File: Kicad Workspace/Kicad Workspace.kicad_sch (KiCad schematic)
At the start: 0 parts

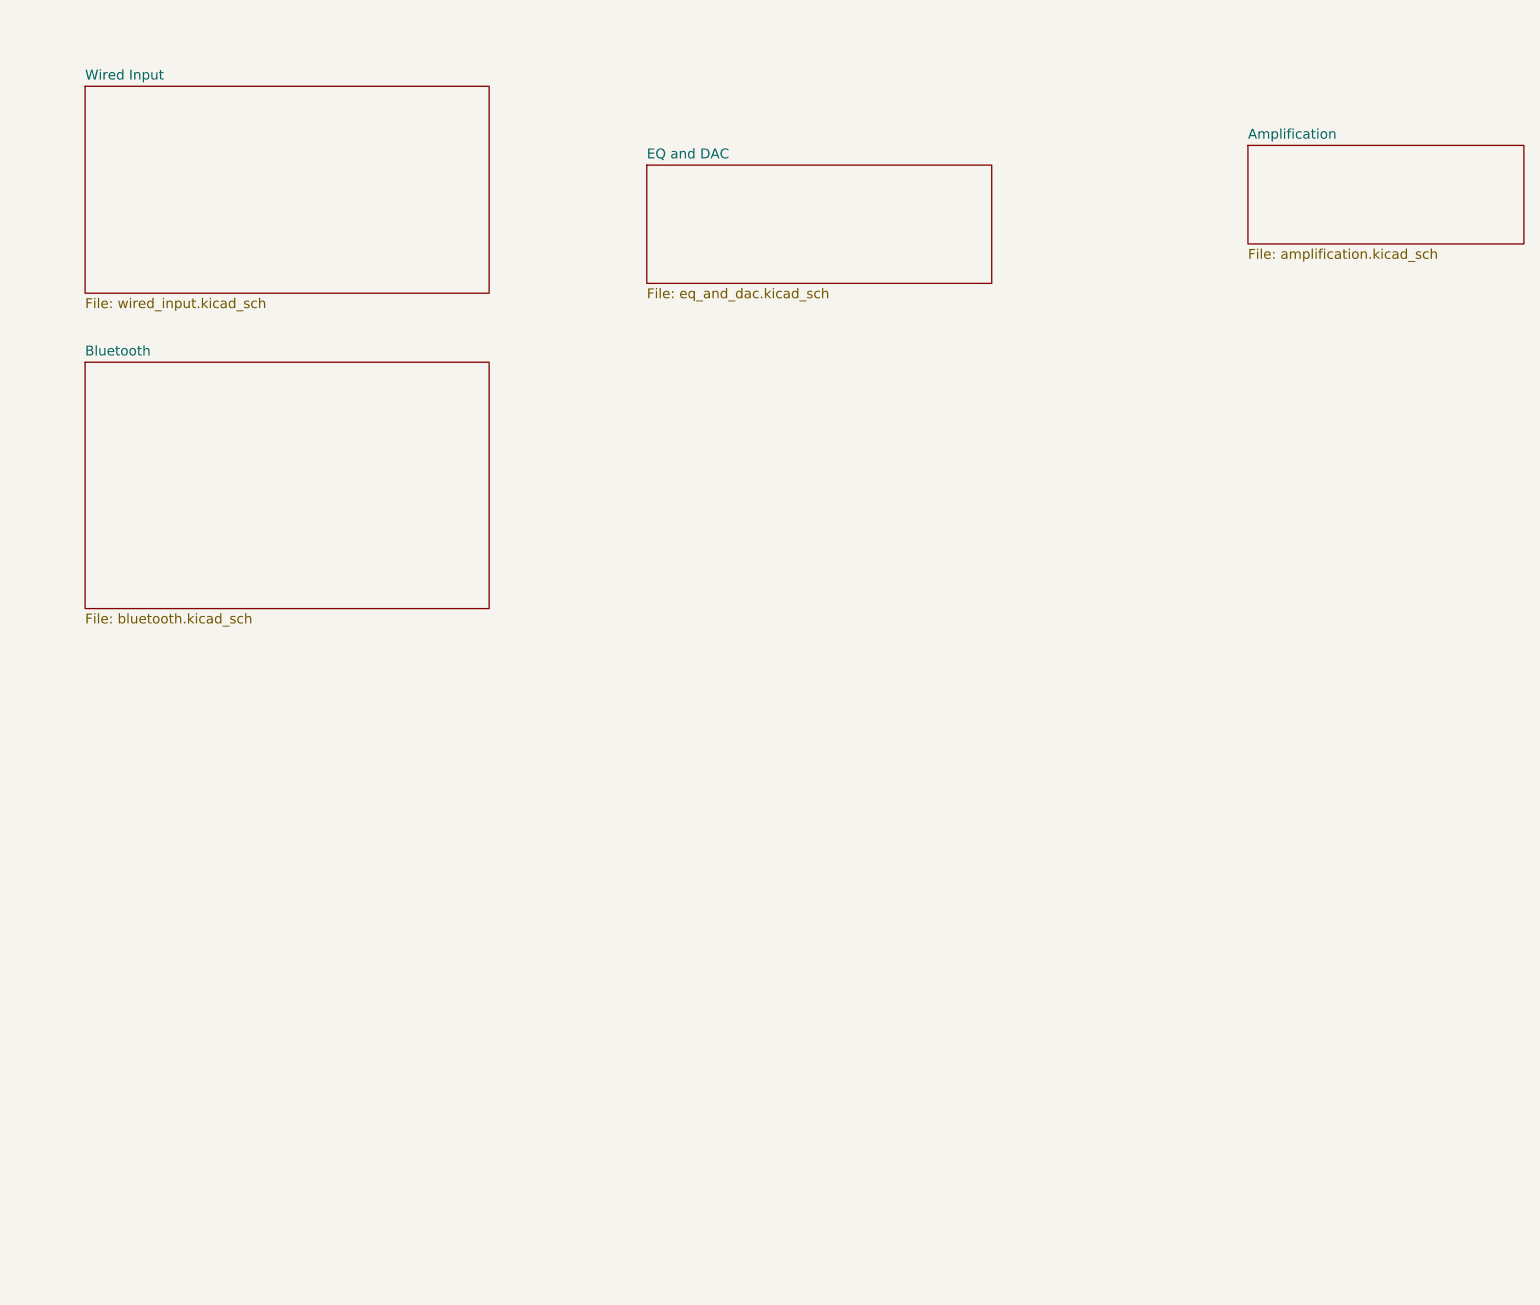
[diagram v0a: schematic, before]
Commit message: Wire input (ADC) schematics done
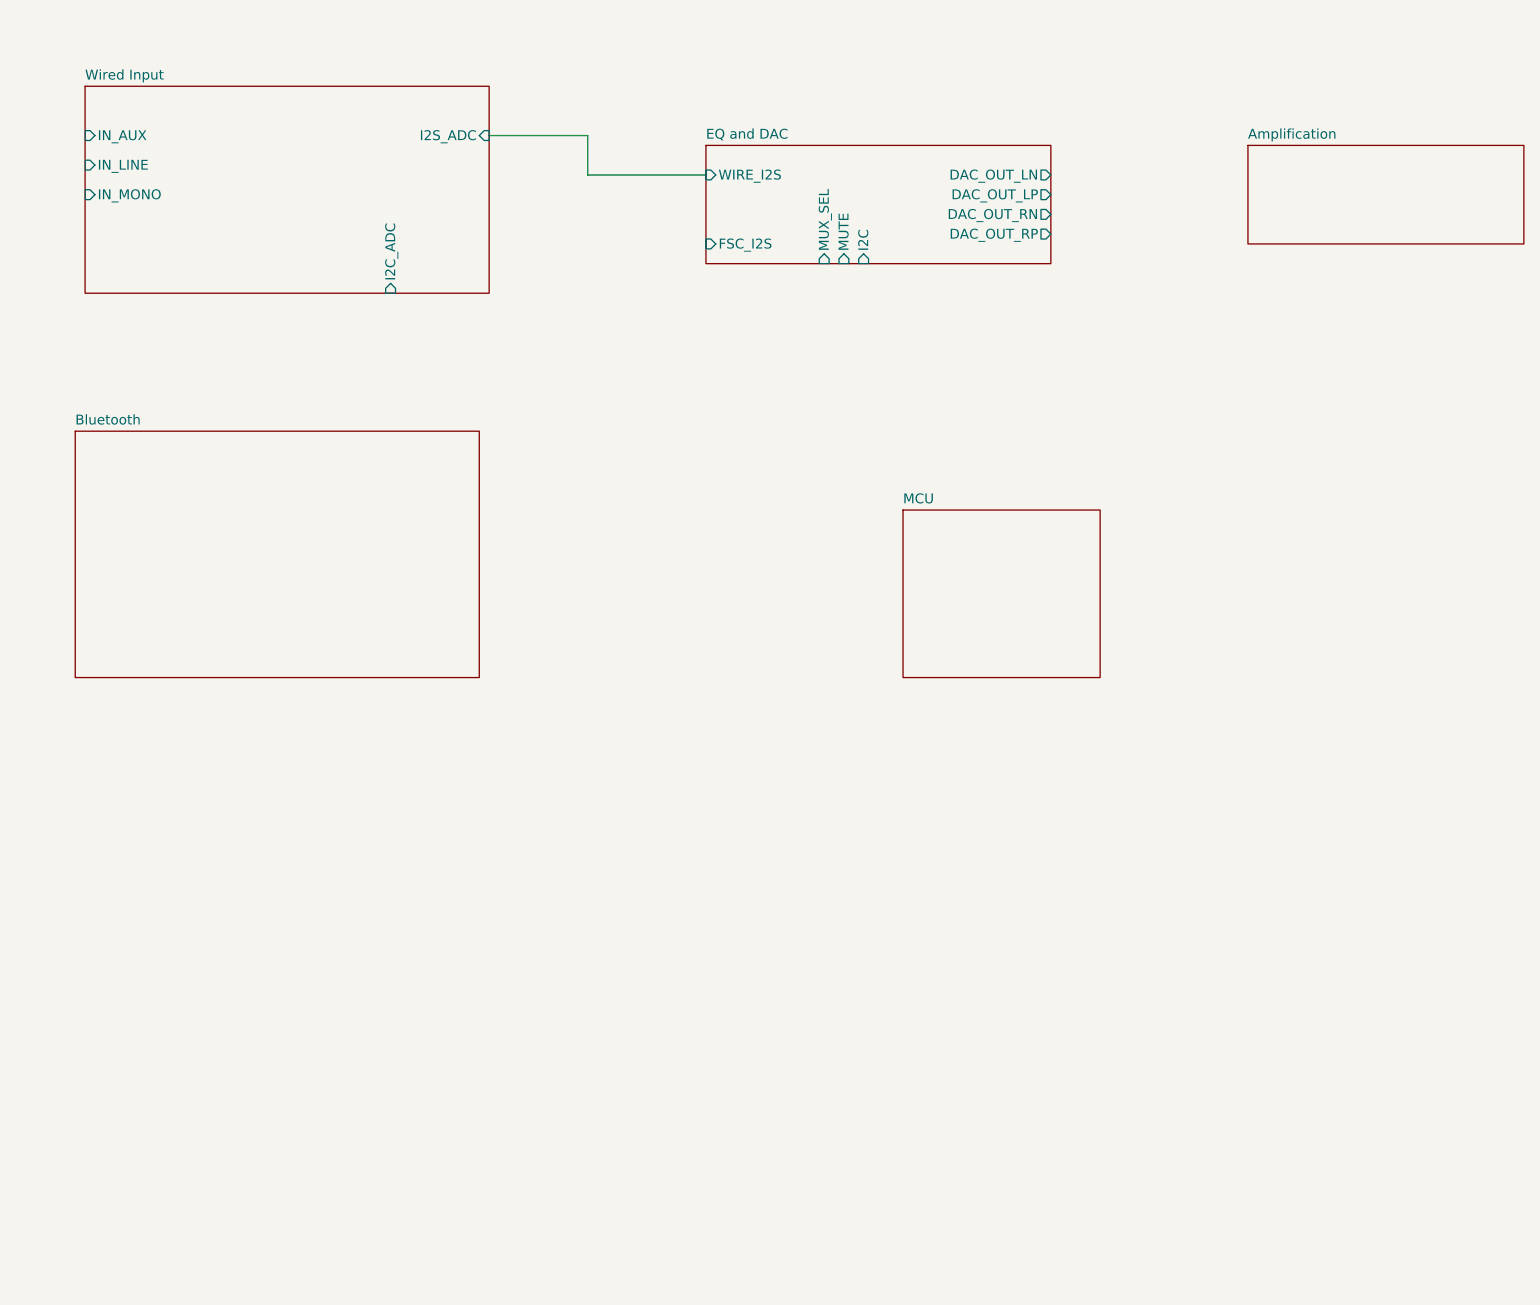
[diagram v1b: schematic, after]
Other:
- added sheet MCU (mcu.kicad_sch)
- sheet EQ and DAC ports: added DAC_OUT_LN, DAC_OUT_LP, DAC_OUT_RN, DAC_OUT_RP, FSC_I2S, I2C, MUTE, MUX_SEL, WIRE_I2S; removed none
- sheet Wired Input ports: added I2C_ADC, I2S_ADC, IN_AUX, IN_LINE, IN_MONO; removed none
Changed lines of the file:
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@@
 	(generator_version "10.0")
 	(paper "A4")
+	(wire
+		(pts
+			(xy 80.01 31.75) (xy 92.71 31.75)
+		)
+		(stroke
+			(width 0)
+			(type default)
+		)
+	)
+	(wire
+		(pts
+			(xy 92.71 36.83) (xy 107.95 36.83)
+		)
+		(stroke
+			(width 0)
+			(type default)
+		)
+	)
+	(wire
+		(pts
+			(xy 92.71 31.75) (xy 92.71 36.83)
+		)
+		(stroke
+			(width 0)
+			(type default)
+		)
+	)
 	(sheet
 		(at 27.94 25.4)
@@
 		(property "Sheetfile" "wired_input.kicad_sch"
 			(at 27.94 52.6546 0)
+			(hide yes)
 			(show_name no)
 			(do_not_autoplace no)
@@
 				)
 				(justify left top)
+			)
+		)
+		(pin "I2C_ADC" input
+			(at 67.31 52.07 270)
+			(effects
+				(font
+					(size 1.27 1.27)
+				)
+				(justify left)
+			)
+		)
+		(pin "I2S_ADC" input
+			(at 80.01 31.75 0)
+			(effects
+				(font
+					(size 1.27 1.27)
+				)
+				(justify right)
+			)
+		)
+		(pin "IN_AUX" input
+			(at 27.94 31.75 180)
+			(effects
+				(font
+					(size 1.27 1.27)
+				)
+				(justify left)
+			)
+		)
+		(pin "IN_LINE" input
+			(at 27.94 35.56 180)
+			(effects
+				(font
+					(size 1.27 1.27)
+				)
+				(justify left)
+			)
+		)
+		(pin "IN_MONO" input
+			(at 27.94 39.37 180)
+			(effects
+				(font
+					(size 1.27 1.27)
+				)
+				(justify left)
 			)
 		)
@@
 	)
 	(sheet
-		(at 100.33 35.56)
+		(at 107.95 33.02)
 		(size 44.45 15.24)
 		(exclude_from_sim no)
@@
 		)
 		(property "Sheetname" "EQ and DAC"
-			(at 100.33 34.8484 0)
+			(at 107.95 32.3084 0)
 			(show_name no)
 			(do_not_autoplace no)
@@
 		)
 		(property "Sheetfile" "eq_and_dac.kicad_sch"
-			(at 100.33 51.3846 0)
+			(at 107.95 48.8446 0)
+			(hide yes)
 			(show_name no)
 			(do_not_autoplace no)
@@
 				)
 				(justify left top)
+			)
+		)
+		(pin "DAC_OUT_LN" output
+			(at 152.4 36.83 0)
+			(effects
+				(font
+					(size 1.27 1.27)
+				)
+				(justify right)
+			)
+		)
+		(pin "DAC_OUT_LP" output
+			(at 152.4 39.37 0)
+			(effects
+				(font
+					(size 1.27 1.27)
+				)
+				(justify right)
+			)
+		)
+		(pin "DAC_OUT_RN" output
+			(at 152.4 41.91 0)
+			(effects
+				(font
+					(size 1.27 1.27)
+				)
+				(justify right)
+			)
+		)
+		(pin "DAC_OUT_RP" output
+			(at 152.4 44.45 0)
+			(effects
+				(font
+					(size 1.27 1.27)
+				)
+				(justify right)
+			)
+		)
+		(pin "FSC_I2S" input
+			(at 107.95 45.72 180)
+			(effects
+				(font
+					(size 1.27 1.27)
+				)
+				(justify left)
+			)
+		)
+		(pin "I2C" input
+			(at 128.27 48.26 270)
+			(effects
+				(font
+					(size 1.27 1.27)
+				)
+				(justify left)
+			)
+		)
+		(pin "MUTE" input
+			(at 125.73 48.26 270)
+			(effects
+				(font
+					(size 1.27 1.27)
+				)
+				(justify left)
+			)
+		)
+		(pin "MUX_SEL" input
+			(at 123.19 48.26 270)
+			(effects
+				(font
+					(size 1.27 1.27)
+				)
+				(justify left)
+			)
+		)
+		(pin "WIRE_I2S" input
+			(at 107.95 36.83 180)
+			(effects
+				(font
+					(size 1.27 1.27)
+				)
+				(justify left)
 			)
 		)
@@
 	)
 	(sheet
-		(at 27.94 60.96)
+		(at 133.35 80.01)
+		(size 25.4 21.59)
+		(exclude_from_sim no)
+		(in_bom yes)
+		(on_board yes)
+		(dnp no)
+		(fields_autoplaced yes)
+		(stroke
+			(width 0.1524)
+			(type solid)
+		)
+		(fill
+			(color 0 0 0 0)
+		)
+		(property "Sheetname" "MCU"
+			(at 133.35 79.2984 0)
+			(show_name no)
+			(do_not_autoplace no)
+			(effects
+				(font
+					(size 1.27 1.27)
+				)
+				(justify left bottom)
+			)
+		)
+		(property "Sheetfile" "mcu.kicad_sch"
+			(at 133.35 102.1846 0)
+			(hide yes)
+			(show_name no)
+			(do_not_autoplace no)
+			(effects
+				(font
+					(size 1.27 1.27)
+				)
+				(justify left top)
+			)
+		)
+		(instances
+			(project "Kicad Workspace"
+				(path "/7c7afbb1-f4ab-42aa-9bad-41afd809eff4"
+					(page "6")
+				)
+			)
+		)
+	)
+	(sheet
+		(at 26.67 69.85)
 		(size 52.07 31.75)
 		(exclude_from_sim no)
@@
 		)
 		(property "Sheetname" "Bluetooth"
-			(at 27.94 60.2484 0)
+			(at 26.67 69.1384 0)
 			(show_name no)
 			(do_not_autoplace no)
@@
 		)
 		(property "Sheetfile" "bluetooth.kicad_sch"
-			(at 27.94 93.2946 0)
+			(at 26.67 102.1846 0)
+			(hide yes)
 			(show_name no)
 			(do_not_autoplace no)
@@
 		(property "Sheetfile" "amplification.kicad_sch"
 			(at 177.8 46.3046 0)
-			(show_name no)
-			(do_not_autoplace no)
+			(hide yes)
+			(show_name no)
+			(do_not_autoplace no)

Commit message: pro and sch update
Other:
- sheet Bluetooth ports: added BT_I2S, BT_RESET, BT_UART; removed none
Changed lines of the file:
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@@
+	(wire
+		(pts
+			(xy 92.71 45.72) (xy 107.95 45.72)
+		)
+		(stroke
+			(width 0)
+			(type default)
+		)
+	)
 	(wire
 		(pts
 			(xy 92.71 31.75) (xy 92.71 36.83)
+		)
+		(stroke
+			(width 0)
+			(type default)
+		)
+	)
+	(wire
+		(pts
+			(xy 78.74 73.66) (xy 92.71 73.66)
+		)
+		(stroke
+			(width 0)
+			(type default)
+		)
+	)
+	(wire
+		(pts
+			(xy 92.71 73.66) (xy 92.71 45.72)
 		)
 		(stroke
@@
 			)
 		)
+		(pin "BT_I2S" output
+			(at 78.74 73.66 0)
+			(effects
+				(font
+					(size 1.27 1.27)
+				)
+				(justify right)
+			)
+		)
+		(pin "BT_RESET" input
+			(at 78.74 99.06 0)
+			(effects
+				(font
+					(size 1.27 1.27)
+				)
+				(justify right)
+			)
+		)
+		(pin "BT_UART" input
+			(at 78.74 96.52 0)
+			(effects
+				(font
+					(size 1.27 1.27)
+				)
+				(justify right)
+			)
+		)
 		(instances
 			(project "Kicad Workspace"
@@
 	)
 	(sheet
-		(at 177.8 33.02)
+		(at 173.99 36.83)
 		(size 35.56 12.7)
 		(exclude_from_sim no)
@@
 		)
 		(property "Sheetname" "Amplification"
-			(at 177.8 32.3084 0)
+			(at 173.99 36.1184 0)
 			(show_name no)
 			(do_not_autoplace no)
@@
 		)
 		(property "Sheetfile" "amplification.kicad_sch"
-			(at 177.8 46.3046 0)
+			(at 173.99 50.1146 0)
 			(hide yes)
 			(show_name no)

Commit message: project update
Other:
- sheet Amplification ports: added CLIP, FAULT, RESET; removed none
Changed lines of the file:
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@@
+			)
+		)
+		(pin "CLIP" output
+			(at 186.69 49.53 270)
+			(effects
+				(font
+					(size 1.27 1.27)
+				)
+				(justify left)
+			)
+		)
+		(pin "FAULT" output
+			(at 189.23 49.53 270)
+			(effects
+				(font
+					(size 1.27 1.27)
+				)
+				(justify left)
+			)
+		)
+		(pin "RESET" input
+			(at 191.77 49.53 270)
+			(effects
+				(font
+					(size 1.27 1.27)
+				)
+				(justify left)
 			)
 		)

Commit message: feat: project global
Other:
- sheet Amplification ports: added IN_L+, IN_L-, IN_R+, IN_R-, L+, L-, R+, R-; removed none
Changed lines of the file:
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@@
 	)
 	(sheet
-		(at 173.99 36.83)
-		(size 35.56 12.7)
+		(at 170.18 27.94)
+		(size 27.94 20.32)
 		(exclude_from_sim no)
 		(in_bom yes)
@@
 		)
 		(property "Sheetname" "Amplification"
-			(at 173.99 36.1184 0)
+			(at 170.18 27.2284 0)
 			(show_name no)
 			(do_not_autoplace no)
@@
 		)
 		(property "Sheetfile" "amplification.kicad_sch"
-			(at 173.99 50.1146 0)
+			(at 170.18 48.8446 0)
 			(hide yes)
 			(show_name no)
@@
 		)
 		(pin "CLIP" output
-			(at 186.69 49.53 270)
+			(at 182.88 48.26 270)
 			(effects
 				(font
@@
 		)
 		(pin "FAULT" output
-			(at 189.23 49.53 270)
+			(at 185.42 48.26 270)
 			(effects
 				(font
@@
 		)
 		(pin "RESET" input
-			(at 191.77 49.53 270)
+			(at 187.96 48.26 270)
 			(effects
 				(font
+					(size 1.27 1.27)
+				)
+				(justify left)
+			)
+		)
+		(pin "IN_L-" input
+			(at 170.18 33.02 180)
+			(effects
+				(font
+					(size 1.27 1.27)
+				)
+				(justify left)
+			)
+		)
+		(pin "IN_R+" input
+			(at 170.18 38.1 180)
+			(effects
+				(font
+					(size 1.27 1.27)
+				)
+				(justify left)
+			)
+		)
+		(pin "IN_R-" input
+			(at 170.18 40.64 180)
+			(effects
+				(font
+					(size 1.27 1.27)
+				)
+				(justify left)
+			)
+		)
+		(pin "L+" output
+			(at 198.12 30.48 0)
+			(effects
+				(font
+					(size 1.27 1.27)
+				)
+				(justify right)
+			)
+		)
+		(pin "L-" output
+			(at 198.12 33.02 0)
+			(effects
+				(font
+					(size 1.27 1.27)
+				)
+				(justify right)
+			)
+		)
+		(pin "R+" output
+			(at 198.12 38.1 0)
+			(effects
+				(font
+					(size 1.27 1.27)
+				)
+				(justify right)
+			)
+		)
+		(pin "R-" output
+			(at 198.12 40.64 0)
+			(effects
+				(font
+					(size 1.27 1.27)
+				)
+				(justify right)
+			)
+		)
+		(pin "IN_L+" input
+			(at 170.18 30.48 180)
+			(effects
+				(font

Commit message: project update
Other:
- added sheet Alimentation (alimentation.kicad_sch)
- sheet EQ and DAC ports: added L+, L-, R+, R-; removed DAC_OUT_LN, DAC_OUT_LP, DAC_OUT_RN, DAC_OUT_RP
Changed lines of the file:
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@@
+	(wire
+		(pts
+			(xy 152.4 35.56) (xy 170.18 35.56)
+		)
+		(stroke
+			(width 0)
+			(type default)
+		)
+	)
 	(wire
 		(pts
@@
 	(wire
 		(pts
+			(xy 152.4 43.18) (xy 170.18 43.18)
+		)
+		(stroke
+			(width 0)
+			(type default)
+		)
+	)
+	(wire
+		(pts
+			(xy 152.4 38.1) (xy 170.18 38.1)
+		)
+		(stroke
+			(width 0)
+			(type default)
+		)
+	)
+	(wire
+		(pts
 			(xy 92.71 31.75) (xy 92.71 36.83)
 		)
@@
 		(pts
 			(xy 78.74 73.66) (xy 92.71 73.66)
+		)
+		(stroke
+			(width 0)
+			(type default)
+		)
+	)
+	(wire
+		(pts
+			(xy 152.4 45.72) (xy 170.18 45.72)
 		)
 		(stroke
@@
 			)
 		)
-		(pin "DAC_OUT_LN" output
-			(at 152.4 36.83 0)
-			(effects
-				(font
-					(size 1.27 1.27)
-				)
-				(justify right)
-			)
-		)
-		(pin "DAC_OUT_LP" output
-			(at 152.4 39.37 0)
-			(effects
-				(font
-					(size 1.27 1.27)
-				)
-				(justify right)
-			)
-		)
-		(pin "DAC_OUT_RN" output
-			(at 152.4 41.91 0)
-			(effects
-				(font
-					(size 1.27 1.27)
-				)
-				(justify right)
-			)
-		)
-		(pin "DAC_OUT_RP" output
-			(at 152.4 44.45 0)
-			(effects
-				(font
-					(size 1.27 1.27)
-				)
-				(justify right)
-			)
-		)
 		(pin "FSC_I2S" input
 			(at 107.95 45.72 180)
@@
 				)
 				(justify left)
+			)
+		)
+		(pin "L+" output
+			(at 152.4 35.56 0)
+			(effects
+				(font
+					(size 1.27 1.27)
+				)
+				(justify right)
+			)
+		)
+		(pin "L-" output
+			(at 152.4 38.1 0)
+			(effects
+				(font
+					(size 1.27 1.27)
+				)
+				(justify right)
+			)
+		)
+		(pin "R+" output
+			(at 152.4 43.18 0)
+			(effects
+				(font
+					(size 1.27 1.27)
+				)
+				(justify right)
+			)
+		)
+		(pin "R-" output
+			(at 152.4 45.72 0)
+			(effects
+				(font
+					(size 1.27 1.27)
+				)
+				(justify right)
 			)
 		)
@@
 	)
 	(sheet
-		(at 170.18 27.94)
+		(at 50.8 156.21)
+		(size 58.42 21.59)
+		(exclude_from_sim no)
+		(in_bom yes)
+		(on_board yes)
+		(dnp no)
+		(fields_autoplaced yes)
+		(stroke
+			(width 0.1524)
+			(type solid)
+		)
+		(fill
+			(color 0 0 0 0)
+		)
+		(property "Sheetname" "Alimentation"
+			(at 50.8 155.4984 0)
+			(show_name no)
+			(do_not_autoplace no)
+			(effects
+				(font
+					(size 1.27 1.27)
+				)
+				(justify left bottom)
+			)
+		)
+		(property "Sheetfile" "alimentation.kicad_sch"
+			(at 50.8 178.3846 0)
+			(show_name no)
+			(do_not_autoplace no)
+			(effects
+				(font
+					(size 1.27 1.27)
+				)
+				(justify left top)
+			)
+		)
+		(instances
+			(project "Kicad Workspace"
+				(path "/7c7afbb1-f4ab-42aa-9bad-41afd809eff4"
+					(page "7")
+				)
+			)
+		)
+	)
+	(sheet
+		(at 170.18 33.02)
 		(size 27.94 20.32)
 		(exclude_from_sim no)
@@
 		)
 		(property "Sheetname" "Amplification"
-			(at 170.18 27.2284 0)
+			(at 170.18 32.3084 0)
 			(show_name no)
 			(do_not_autoplace no)
@@
 		)
 		(property "Sheetfile" "amplification.kicad_sch"
-			(at 170.18 48.8446 0)
+			(at 170.18 53.9246 0)
 			(hide yes)
 			(show_name no)
@@
 		)
 		(pin "CLIP" output
-			(at 182.88 48.26 270)
+			(at 182.88 53.34 270)
 			(effects
 				(font
@@
 		)
 		(pin "FAULT" output
-			(at 185.42 48.26 270)
+			(at 185.42 53.34 270)
 			(effects
 				(font
@@
 		)
 		(pin "RESET" input
-			(at 187.96 48.26 270)
+			(at 187.96 53.34 270)
 			(effects
 				(font
@@
 		)
 		(pin "IN_L-" input
-			(at 170.18 33.02 180)
+			(at 170.18 38.1 180)
 			(effects
 				(font
@@
 		)
 		(pin "IN_R+" input
-			(at 170.18 38.1 180)
+			(at 170.18 43.18 180)
 			(effects
 				(font
@@
 		)
 		(pin "IN_R-" input
-			(at 170.18 40.64 180)
+			(at 170.18 45.72 180)
 			(effects
 				(font
@@
 		)
 		(pin "L+" output
-			(at 198.12 30.48 0)
+			(at 198.12 35.56 0)
 			(effects
 				(font
@@
 		)
 		(pin "L-" output
-			(at 198.12 33.02 0)
+			(at 198.12 38.1 0)
 			(effects
 				(font
@@
 		)
 		(pin "R+" output
-			(at 198.12 38.1 0)
+			(at 198.12 43.18 0)
 			(effects
 				(font
@@
 		)
 		(pin "R-" output
-			(at 198.12 40.64 0)
+			(at 198.12 45.72 0)
 			(effects
 				(font
@@
 		)
 		(pin "IN_L+" input
-			(at 170.18 30.48 180)
-			(effects
-				(font
+			(at 170.18 35.56 180)
+			(effects
+				(font

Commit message: feat: schematics almost done, starting to correct compile pb
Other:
- sheet Bluetooth ports: added BT_I2S{BT_BCK BT_DATA BT_LRCK}, UART{TX RX CTS RTS}; removed BT_I2S, BT_UART
- sheet EQ and DAC ports: added BT_I2S{BT_DATA BT_BCK BT_LRCK}, I2C{SCL SDA}, WIRE_I2S{WIRE_DATA WIRE_BCK WIRE_LRCK}; removed FSC_I2S, I2C, WIRE_I2S
- sheet MCU ports: added FAULT_AMP, I2C, MUTE_DAC, MUX_SEL, RESET_AMP, RESET_BT, UART{TX RX CTS RTS}; removed none
- sheet Wired Input ports: added AUX, LINE, MONO, WIRE_I2S{WIRE_DATA WIRE_BCK WIRE_LRCK}; removed I2C_ADC, I2S_ADC, IN_AUX, IN_LINE, IN_MONO

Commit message: project update
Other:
- sheet MCU ports: added I2C{SCL SDA}; removed I2C
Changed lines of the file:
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@@
 			)
 		)
-		(pin "I2C" bidirectional
+		(pin "I2C{SCL SDA}" bidirectional
 			(at 123.19 77.47 90)
 			(effects

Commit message: project update
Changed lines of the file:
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@@
 	)
 	(sheet
-		(at 50.8 156.21)
+		(at 34.29 127)
 		(size 58.42 21.59)
 		(exclude_from_sim no)
@@
 		)
 		(property "Sheetname" "Alimentation"
-			(at 50.8 155.4984 0)
+			(at 34.29 126.2884 0)
 			(show_name no)
 			(do_not_autoplace no)
@@
 		)
 		(property "Sheetfile" "alimentation.kicad_sch"
-			(at 50.8 178.3846 0)
+			(at 34.29 149.1746 0)
 			(show_name no)
 			(do_not_autoplace no)
